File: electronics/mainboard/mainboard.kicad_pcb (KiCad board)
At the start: 2 copper layers, 1 part

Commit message: add terminals
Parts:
- added J1: Conn_01x09, Wuerth:691247510009, F.Cu at (224.5, 118.2)
- added J2: Conn_01x09, Wuerth:691247510009, F.Cu at (209.2, 118.2)

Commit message: place parts
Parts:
- added J3: Conn_01x09, Wuerth:691247510009, F.Cu at (178.8, 91.3)
- added J4: Conn_01x09, Wuerth:691247510009, F.Cu at (163.5, 91.3)
- added J5: Conn_01x09, Wuerth:691247510009, F.Cu at (148.3, 91.3)
- added J6: Conn_01x09, Wuerth:691247510009, F.Cu at (133.1, 91.3)
- added J7: Conn_01x09, Wuerth:691247510009, F.Cu at (117.8, 91.3)
- added J8: Conn_01x09, Wuerth:691247510009, F.Cu at (102.6, 91.3)
- added J9: Conn_01x09, Wuerth:691247510009, F.Cu at (87.3, 91.3)
- added J99: Conn_01x08, Connector_PinHeader_2.54mm:PinHeader_1x08_P2.54mm_Vertical_SMD_Pin1Right, B.Cu at (156.8, 111.1)
- moved XA1 62.0 mm to (97.2, 113.7)
- moved J1 27.6 mm to (218.1, 91.3), turned to 180 degrees
- moved J2 27.6 mm to (202.9, 91.3), turned to 180 degrees
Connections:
- XA1 pad A0: unconnected-(XA1-PadA0) -> Net-(XA1-PadA0)
- XA1 pad A1: unconnected-(XA1-PadA1) -> Net-(XA1-PadA1)
- XA1 pad A2: unconnected-(XA1-PadA2) -> Net-(XA1-PadA2)
- XA1 pad A3: unconnected-(XA1-PadA3) -> Net-(XA1-PadA3)
- XA1 pad A4: unconnected-(XA1-PadA4) -> Net-(XA1-PadA4)
- XA1 pad A5: unconnected-(XA1-PadA5) -> Net-(XA1-PadA5)
- XA1 pad A6: unconnected-(XA1-PadA6) -> Net-(XA1-PadA6)
- XA1 pad A7: unconnected-(XA1-PadA7) -> Net-(XA1-PadA7)
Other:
- board outline added: 151.1 x 55.9 mm

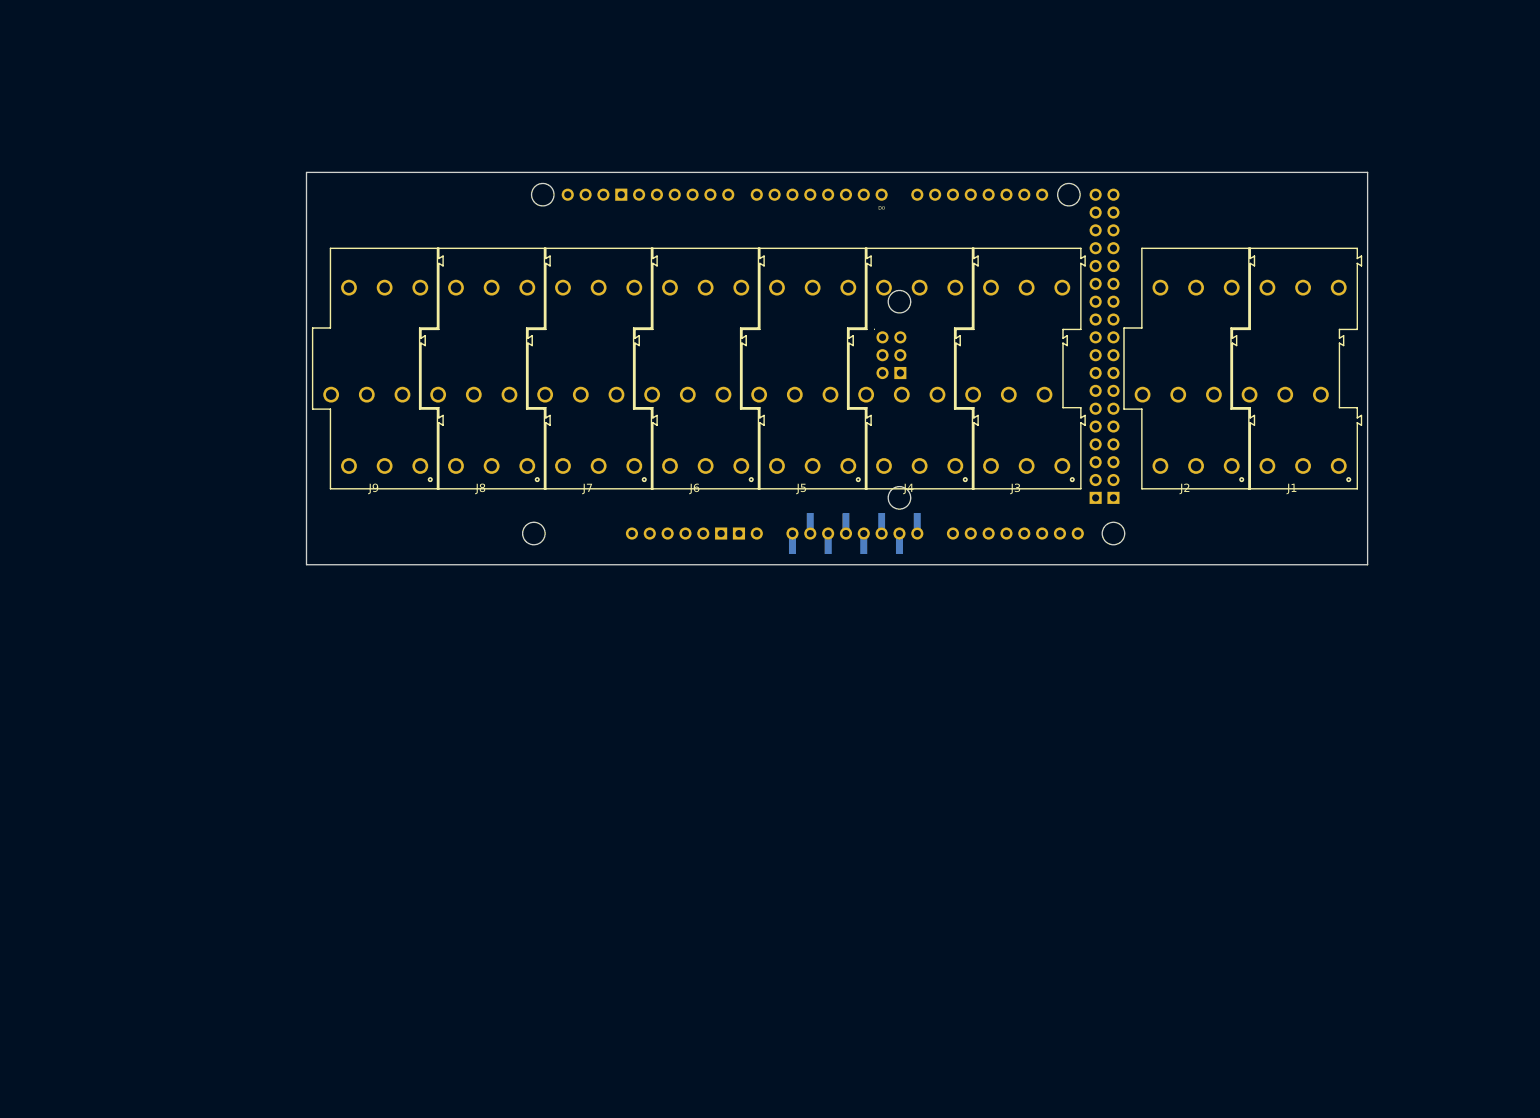
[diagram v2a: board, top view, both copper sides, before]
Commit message: add and wire parts in schematic
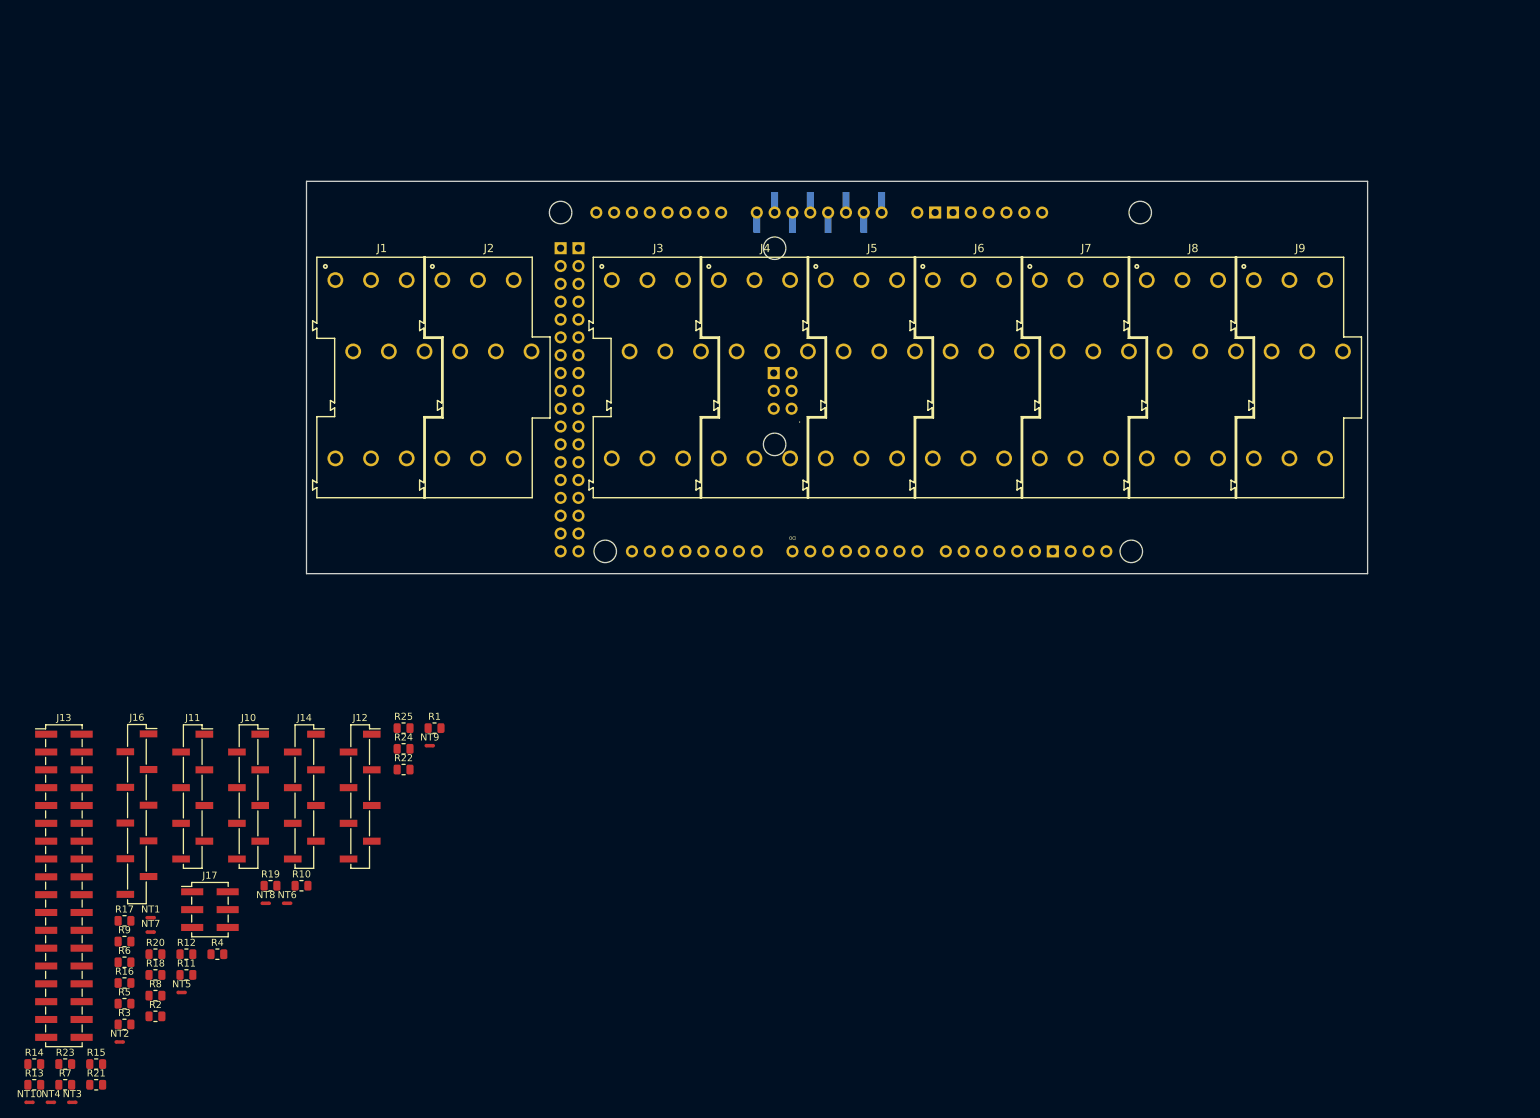
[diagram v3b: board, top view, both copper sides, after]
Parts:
- added J10: Conn_01x08, Connector_PinHeader_2.54mm:PinHeader_1x08_P2.54mm_Vertical_SMD_Pin1Right, F.Cu at (70.5, 148.6)
- added J11: Conn_01x08, Connector_PinHeader_2.54mm:PinHeader_1x08_P2.54mm_Vertical_SMD_Pin1Right, F.Cu at (62.5, 148.6)
- added J12: Conn_01x08, Connector_PinHeader_2.54mm:PinHeader_1x08_P2.54mm_Vertical_SMD_Pin1Right, F.Cu at (86.4, 148.6)
- added J13: Conn_02x18_Odd_Even, Connector_PinHeader_2.54mm:PinHeader_2x18_P2.54mm_Vertical_SMD, F.Cu at (44.2, 161.3)
- added J14: Conn_01x08, Connector_PinHeader_2.54mm:PinHeader_1x08_P2.54mm_Vertical_SMD_Pin1Right, F.Cu at (78.4, 148.6)
- added J16: Conn_01x10, Connector_PinHeader_2.54mm:PinHeader_1x10_P2.54mm_Vertical_SMD_Pin1Right, F.Cu at (54.6, 151.1)
- added J17: Conn_02x03_Odd_Even, Connector_PinHeader_2.54mm:PinHeader_2x03_P2.54mm_Vertical_SMD, F.Cu at (65.0, 164.7)
- added NT1: NetTie_2, NetTie:NetTie-2_SMD_Pad0.5mm, F.Cu at (56.5, 165.8)
- added NT10: NetTie_2, NetTie:NetTie-2_SMD_Pad0.5mm, F.Cu at (39.3, 192.1)
- added NT2: NetTie_2, NetTie:NetTie-2_SMD_Pad0.5mm, F.Cu at (52.1, 183.5)
- added NT3: NetTie_2, NetTie:NetTie-2_SMD_Pad0.5mm, F.Cu at (45.4, 192.1)
- added NT4: NetTie_2, NetTie:NetTie-2_SMD_Pad0.5mm, F.Cu at (42.3, 192.1)
- added NT5: NetTie_2, NetTie:NetTie-2_SMD_Pad0.5mm, F.Cu at (61.0, 176.5)
- added NT6: NetTie_2, NetTie:NetTie-2_SMD_Pad0.5mm, F.Cu at (76.0, 163.8)
- added NT7: NetTie_2, NetTie:NetTie-2_SMD_Pad0.5mm, F.Cu at (56.5, 167.9)
- added NT8: NetTie_2, NetTie:NetTie-2_SMD_Pad0.5mm, F.Cu at (72.9, 163.8)
- added NT9: NetTie_2, NetTie:NetTie-2_SMD_Pad0.5mm, F.Cu at (96.3, 141.3)
- added R1: 0, Resistor_SMD:R_0805_2012Metric, F.Cu at (97.0, 138.8)
- added R10: 0, Resistor_SMD:R_0805_2012Metric, F.Cu at (78.0, 161.3)
- added R11: 0, Resistor_SMD:R_0805_2012Metric, F.Cu at (61.6, 174.0)
- added R12: 0, Resistor_SMD:R_0805_2012Metric, F.Cu at (61.6, 171.0)
- added R13: 0, Resistor_SMD:R_0805_2012Metric, F.Cu at (40.0, 189.6)
- added R14: 0, Resistor_SMD:R_0805_2012Metric, F.Cu at (40.0, 186.7)
- added R15: 0, Resistor_SMD:R_0805_2012Metric, F.Cu at (48.8, 186.7)
- added R16: 0, Resistor_SMD:R_0805_2012Metric, F.Cu at (52.8, 175.1)
- added R17: 0, Resistor_SMD:R_0805_2012Metric, F.Cu at (52.8, 166.3)
- added R18: 0, Resistor_SMD:R_0805_2012Metric, F.Cu at (57.2, 174.0)
- added R19: 0, Resistor_SMD:R_0805_2012Metric, F.Cu at (73.6, 161.3)
- added R2: 0, Resistor_SMD:R_0805_2012Metric, F.Cu at (57.2, 179.9)
- added R20: 0, Resistor_SMD:R_0805_2012Metric, F.Cu at (57.2, 171.0)
- added R21: 0, Resistor_SMD:R_0805_2012Metric, F.Cu at (48.8, 189.6)
- added R22: 0, Resistor_SMD:R_0805_2012Metric, F.Cu at (92.6, 144.7)
- added R23: 0, Resistor_SMD:R_0805_2012Metric, F.Cu at (44.4, 186.7)
- added R24: 0, Resistor_SMD:R_0805_2012Metric, F.Cu at (92.6, 141.8)
- added R25: 0, Resistor_SMD:R_0805_2012Metric, F.Cu at (92.6, 138.8)
- added R3: 0, Resistor_SMD:R_0805_2012Metric, F.Cu at (52.8, 181.0)
- added R4: 0, Resistor_SMD:R_0805_2012Metric, F.Cu at (66.0, 171.0)
- added R5: 0, Resistor_SMD:R_0805_2012Metric, F.Cu at (52.8, 178.1)
- added R6: 0, Resistor_SMD:R_0805_2012Metric, F.Cu at (52.8, 172.2)
- added R7: 0, Resistor_SMD:R_0805_2012Metric, F.Cu at (44.4, 189.6)
- added R8: 0, Resistor_SMD:R_0805_2012Metric, F.Cu at (57.2, 176.9)
- added R9: 0, Resistor_SMD:R_0805_2012Metric, F.Cu at (52.8, 169.2)
- moved J9 134.1 mm to (221.3, 85.2), turned to 0 degrees
- moved J1 127.8 mm to (90.5, 85.2), turned to 0 degrees
- moved XA1 125.1 mm to (211.5, 62.9), turned to 180 degrees
- moved J8 103.7 mm to (206.0, 85.2), turned to 0 degrees
- moved J2 97.4 mm to (105.7, 85.2), turned to 0 degrees
- moved J7 73.2 mm to (190.8, 85.2), turned to 0 degrees
- moved J3 49.3 mm to (129.8, 85.2), turned to 0 degrees
- moved J15 46.0 mm to (151.8, 65.4), turned to 90 degrees
- moved J6 43.0 mm to (175.6, 85.2), turned to 0 degrees
- moved J4 19.5 mm to (145.1, 85.2), turned to 0 degrees
- moved J5 13.5 mm to (160.3, 85.2), turned to 0 degrees
- renumbered J99 to J15
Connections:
- J1 pad 1: unconnected-(J1-Pad1) -> +5V
- J1 pad 2: unconnected-(J1-Pad2) -> /Leds1
- J1 pad 3: unconnected-(J1-Pad3) -> GND
- J1 pad 4: unconnected-(J1-Pad4) -> +5V
- J1 pad 5: unconnected-(J1-Pad5) -> /Leds2
- J1 pad 6: unconnected-(J1-Pad6) -> GND
- J1 pad 7: unconnected-(J1-Pad7) -> +5V
- J1 pad 8: unconnected-(J1-Pad8) -> /Leds3
- J1 pad 9: unconnected-(J1-Pad9) -> GND
- J15 pad 1: Net-(XA1-PadA0) -> /D7
- J15 pad 2: Net-(XA1-PadA1) -> /D6
- J15 pad 3: Net-(XA1-PadA2) -> /D5
- J15 pad 4: Net-(XA1-PadA3) -> /D4
- J15 pad 5: Net-(XA1-PadA4) -> /D3
- J15 pad 6: Net-(XA1-PadA5) -> /D2
- J15 pad 7: Net-(XA1-PadA6) -> /D1
- J15 pad 8: Net-(XA1-PadA7) -> /D0
- J2 pad 1: unconnected-(J2-Pad1) -> +5V
- J2 pad 2: unconnected-(J2-Pad2) -> /Leds4
- J2 pad 3: unconnected-(J2-Pad3) -> GND
- J2 pad 4: unconnected-(J2-Pad4) -> +5V
- J2 pad 5: unconnected-(J2-Pad5) -> /Leds5
- J2 pad 6: unconnected-(J2-Pad6) -> GND
- J2 pad 7: unconnected-(J2-Pad7) -> +5V
- J2 pad 8: unconnected-(J2-Pad8) -> /Leds6
- J2 pad 9: unconnected-(J2-Pad9) -> GND
- J3 pad 1: unconnected-(J3-Pad1) -> +5V
- J3 pad 2: unconnected-(J3-Pad2) -> /Leds7
- J3 pad 3: unconnected-(J3-Pad3) -> GND
- J3 pad 4: unconnected-(J3-Pad4) -> +5V
- J3 pad 5: unconnected-(J3-Pad5) -> /Leds8
- J3 pad 6: unconnected-(J3-Pad6) -> GND
- J3 pad 7: unconnected-(J3-Pad7) -> +5V
- J3 pad 8: unconnected-(J3-Pad8) -> /Leds9
- J3 pad 9: unconnected-(J3-Pad9) -> GND
- J4 pad 1: unconnected-(J4-Pad1) -> +5V
- J4 pad 2: unconnected-(J4-Pad2) -> /Leds10
- J4 pad 3: unconnected-(J4-Pad3) -> GND
- J4 pad 4: unconnected-(J4-Pad4) -> +5V
- J4 pad 5: unconnected-(J4-Pad5) -> /Leds11
- J4 pad 6: unconnected-(J4-Pad6) -> GND
- J4 pad 7: unconnected-(J4-Pad7) -> +5V
- J4 pad 8: unconnected-(J4-Pad8) -> /Leds12
- J4 pad 9: unconnected-(J4-Pad9) -> GND
- J5 pad 1: unconnected-(J5-Pad1) -> +5V
- J5 pad 2: unconnected-(J5-Pad2) -> /Leds13
- J5 pad 3: unconnected-(J5-Pad3) -> GND
- J5 pad 4: unconnected-(J5-Pad4) -> +5V
- J5 pad 5: unconnected-(J5-Pad5) -> /Leds14
- J5 pad 6: unconnected-(J5-Pad6) -> GND
- J5 pad 7: unconnected-(J5-Pad7) -> +5V
- J5 pad 8: unconnected-(J5-Pad8) -> /Leds15
- J5 pad 9: unconnected-(J5-Pad9) -> GND
- J6 pad 1: unconnected-(J6-Pad1) -> +5V
- J6 pad 2: unconnected-(J6-Pad2) -> /Leds16
- J6 pad 3: unconnected-(J6-Pad3) -> GND
- J6 pad 4: unconnected-(J6-Pad4) -> +5V
- J6 pad 5: unconnected-(J6-Pad5) -> /Leds17
- J6 pad 6: unconnected-(J6-Pad6) -> GND
- J6 pad 7: unconnected-(J6-Pad7) -> +5V
- J6 pad 8: unconnected-(J6-Pad8) -> /Leds18
- J6 pad 9: unconnected-(J6-Pad9) -> GND
- J7 pad 1: unconnected-(J7-Pad1) -> +5V
- J7 pad 2: unconnected-(J7-Pad2) -> /Leds19
- J7 pad 3: unconnected-(J7-Pad3) -> GND
- J7 pad 4: unconnected-(J7-Pad4) -> +5V
- J7 pad 5: unconnected-(J7-Pad5) -> /Leds20
- J7 pad 6: unconnected-(J7-Pad6) -> GND
- J7 pad 7: unconnected-(J7-Pad7) -> +5V
- J7 pad 8: unconnected-(J7-Pad8) -> /Leds21
- J7 pad 9: unconnected-(J7-Pad9) -> GND
- J8 pad 1: unconnected-(J8-Pad1) -> +5V
- J8 pad 2: unconnected-(J8-Pad2) -> /Leds22
- J8 pad 3: unconnected-(J8-Pad3) -> GND
- J8 pad 4: unconnected-(J8-Pad4) -> +5V
- J8 pad 5: unconnected-(J8-Pad5) -> /Leds23
- J8 pad 6: unconnected-(J8-Pad6) -> GND
- J8 pad 7: unconnected-(J8-Pad7) -> +5V
- J8 pad 8: unconnected-(J8-Pad8) -> /Leds24
- J8 pad 9: unconnected-(J8-Pad9) -> GND
- J9 pad 1: unconnected-(J9-Pad1) -> +5V
- J9 pad 2: unconnected-(J9-Pad2) -> /Leds25
- J9 pad 3: unconnected-(J9-Pad3) -> GND
- J9 pad 4: unconnected-(J9-Pad4) -> +5V
- J9 pad 6: unconnected-(J9-Pad6) -> GND
- J9 pad 7: unconnected-(J9-Pad7) -> +5V
- J9 pad 9: unconnected-(J9-Pad9) -> GND
- XA1 pad 3V3: unconnected-(XA1-Pad3V3) -> /3V3
- XA1 pad 5V1: unconnected-(XA1-Pad5V1) -> /5V1
- XA1 pad 5V2: unconnected-(XA1-Pad5V2) -> /5V2
- XA1 pad 5V3: unconnected-(XA1-Pad5V3) -> /5V3
- XA1 pad 5V4: unconnected-(XA1-Pad5V4) -> /5V4
- XA1 pad A0: Net-(XA1-PadA0) -> /A0
- XA1 pad A1: Net-(XA1-PadA1) -> /A1
- XA1 pad A10: unconnected-(XA1-PadA10) -> /A10
- XA1 pad A11: unconnected-(XA1-PadA11) -> /A11
- XA1 pad A12: unconnected-(XA1-PadA12) -> /A12
- XA1 pad A13: unconnected-(XA1-PadA13) -> /A13
- XA1 pad A14: unconnected-(XA1-PadA14) -> /A14
- XA1 pad A15: unconnected-(XA1-PadA15) -> /A15
- XA1 pad A2: Net-(XA1-PadA2) -> /A2
- XA1 pad A3: Net-(XA1-PadA3) -> /A3
- XA1 pad A4: Net-(XA1-PadA4) -> /A4
- XA1 pad A5: Net-(XA1-PadA5) -> /A5
- XA1 pad A6: Net-(XA1-PadA6) -> /A6
- XA1 pad A7: Net-(XA1-PadA7) -> /A7
- XA1 pad A8: unconnected-(XA1-PadA8) -> /A8
- XA1 pad A9: unconnected-(XA1-PadA9) -> /A9
- XA1 pad AREF: unconnected-(XA1-PadAREF) -> /AREF
- XA1 pad D0: unconnected-(XA1-PadD0) -> /D0
- XA1 pad D1: unconnected-(XA1-PadD1) -> /D1
- XA1 pad D10: unconnected-(XA1-PadD10) -> /D10
- XA1 pad D11: unconnected-(XA1-PadD11) -> /D11
- XA1 pad D12: unconnected-(XA1-PadD12) -> /D12
- XA1 pad D13: unconnected-(XA1-PadD13) -> /D13
- XA1 pad D14: unconnected-(XA1-PadD14) -> /D14
- XA1 pad D15: unconnected-(XA1-PadD15) -> /D15
- XA1 pad D16: unconnected-(XA1-PadD16) -> /D16
- XA1 pad D17: unconnected-(XA1-PadD17) -> /D17
- XA1 pad D18: unconnected-(XA1-PadD18) -> /D18
- XA1 pad D19: unconnected-(XA1-PadD19) -> /D19
- XA1 pad D2: unconnected-(XA1-PadD2) -> /D2
- XA1 pad D20: unconnected-(XA1-PadD20) -> /D20
- XA1 pad D21: unconnected-(XA1-PadD21) -> /D21
- XA1 pad D22: unconnected-(XA1-PadD22) -> /D22
- XA1 pad D23: unconnected-(XA1-PadD23) -> /D23
- XA1 pad D24: unconnected-(XA1-PadD24) -> /D24
- XA1 pad D25: unconnected-(XA1-PadD25) -> /D25
- XA1 pad D26: unconnected-(XA1-PadD26) -> /D26
- XA1 pad D27: unconnected-(XA1-PadD27) -> /D27
- XA1 pad D28: unconnected-(XA1-PadD28) -> /D28
- XA1 pad D29: unconnected-(XA1-PadD29) -> /D29
- XA1 pad D3: unconnected-(XA1-PadD3) -> /D3
- XA1 pad D30: unconnected-(XA1-PadD30) -> /D30
- XA1 pad D31: unconnected-(XA1-PadD31) -> /D31
- XA1 pad D32: unconnected-(XA1-PadD32) -> /D32
- XA1 pad D33: unconnected-(XA1-PadD33) -> /D33
- XA1 pad D34: unconnected-(XA1-PadD34) -> /D34
- XA1 pad D35: unconnected-(XA1-PadD35) -> /D35
- XA1 pad D36: unconnected-(XA1-PadD36) -> /D36
- XA1 pad D37: unconnected-(XA1-PadD37) -> /D37
- XA1 pad D38: unconnected-(XA1-PadD38) -> /D38
- XA1 pad D39: unconnected-(XA1-PadD39) -> /D39
- XA1 pad D4: unconnected-(XA1-PadD4) -> /D4
- XA1 pad D40: unconnected-(XA1-PadD40) -> /D40
- XA1 pad D41: unconnected-(XA1-PadD41) -> /D41
- XA1 pad D42: unconnected-(XA1-PadD42) -> /D42
- XA1 pad D43: unconnected-(XA1-PadD43) -> /D43
- XA1 pad D44: unconnected-(XA1-PadD44) -> /D44
- XA1 pad D45: unconnected-(XA1-PadD45) -> /D45
- XA1 pad D46: unconnected-(XA1-PadD46) -> /D46
- XA1 pad D47: unconnected-(XA1-PadD47) -> /D47
- XA1 pad D48: unconnected-(XA1-PadD48) -> /D48
- XA1 pad D49: unconnected-(XA1-PadD49) -> /D49
- XA1 pad D5: unconnected-(XA1-PadD5) -> /D5
- XA1 pad D50: unconnected-(XA1-PadD50) -> /D50
- XA1 pad D51: unconnected-(XA1-PadD51) -> /D51
- XA1 pad D52: unconnected-(XA1-PadD52) -> /D52
- XA1 pad D53: unconnected-(XA1-PadD53) -> /D53
- XA1 pad D6: unconnected-(XA1-PadD6) -> /D6
- XA1 pad D7: unconnected-(XA1-PadD7) -> /D7
- XA1 pad D8: unconnected-(XA1-PadD8) -> /D8
- XA1 pad D9: unconnected-(XA1-PadD9) -> /D9
- XA1 pad GND1: unconnected-(XA1-PadGND1) -> /GND1
- XA1 pad GND2: unconnected-(XA1-PadGND2) -> /GND2
- XA1 pad GND3: unconnected-(XA1-PadGND3) -> /GND3
- XA1 pad GND4: unconnected-(XA1-PadGND4) -> /GND4
- XA1 pad GND5: unconnected-(XA1-PadGND5) -> /GND5
- XA1 pad GND6: unconnected-(XA1-PadGND6) -> /GND6
- XA1 pad IORF: unconnected-(XA1-PadIORF) -> /IORF
- XA1 pad MISO: unconnected-(XA1-PadMISO) -> /MISO
- XA1 pad MOSI: unconnected-(XA1-PadMOSI) -> /MOSI
- XA1 pad RST1: unconnected-(XA1-PadRST1) -> /RST1
- XA1 pad RST2: unconnected-(XA1-PadRST2) -> /RST2
- XA1 pad SCK: unconnected-(XA1-PadSCK) -> /SCK
- XA1 pad SCL: unconnected-(XA1-PadSCL) -> /SCL
- XA1 pad SDA: unconnected-(XA1-PadSDA) -> /SDA
- XA1 pad VIN: unconnected-(XA1-PadVIN) -> /VIN

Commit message: place parts on pcb
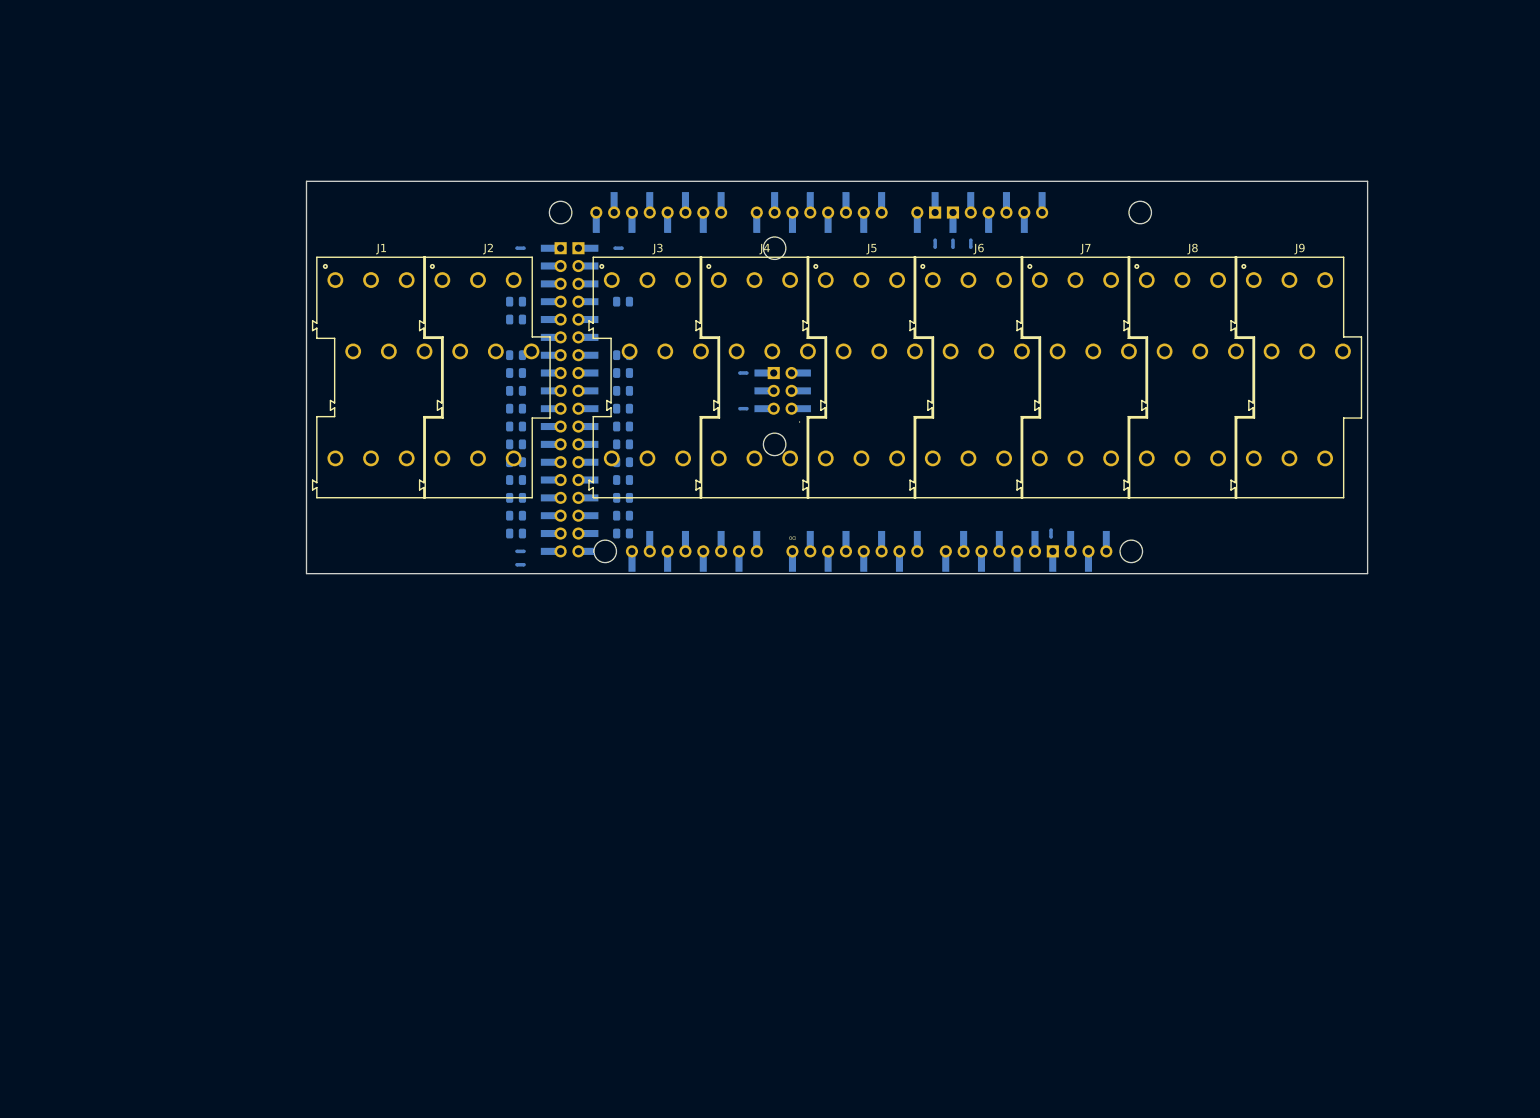
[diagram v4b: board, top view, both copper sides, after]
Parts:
- J10, J11, J12, J13, J14, J16, NT1, NT10, NT2, NT3, NT4, NT5, NT6, NT7, NT8, NT9, R1, R10, R11, R12, R13, R14, R15, R16, R17, R18, R19, R2, R20, R21, R22, R23, R24, R25, R3, R4, R5, R6, R7, R8, R9: moved to B.Cu
- J17: footprint Connector_PinHeader_2.54mm:PinHeader_2x03_P2.54mm_Vertical_SMD -> Connector_PinSocket_2.54mm:PinSocket_2x03_P2.54mm_Vertical_SMD; moved to B.Cu
- moved NT1 151.2 mm to (173.4, 69.8), turned to 90 degrees
- moved NT7 148.6 mm to (168.3, 69.8), turned to 90 degrees
- moved NT10 140.3 mm to (109.2, 70.5)
- moved NT5 140.0 mm to (184.8, 111.1), turned to -90 degrees
- moved NT6 133.5 mm to (170.8, 69.8), turned to 90 degrees
- moved J10 133.3 mm to (174.6, 65.4), turned to 90 degrees
- moved J16 132.1 mm to (181.2, 113.7), turned to 90 degrees
- moved R21 128.2 mm to (123.8, 85.7), turned to 180 degrees
- moved NT2 126.6 mm to (141.0, 93.3)
- moved R13 125.8 mm to (123.8, 95.9), turned to 180 degrees
- moved R23 124.0 mm to (108.6, 80.6)
- moved J11 122.0 mm to (151.8, 65.4), turned to 90 degrees
- moved R15 119.8 mm to (123.8, 93.3), turned to 180 degrees
- moved R7 117.2 mm to (123.8, 103.5), turned to 180 degrees
- moved R14 113.8 mm to (108.6, 95.9)
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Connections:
- J13 pad 1: /5V3 -> /5V4
- J13 pad 10: /D29 -> /D28
- J13 pad 11: /D30 -> /D31
- J13 pad 12: /D31 -> /D30
- J13 pad 13: /D32 -> /D33
- J13 pad 14: /D33 -> /D32
- J13 pad 15: /D34 -> /D35
- J13 pad 16: /D35 -> /D34
- J13 pad 17: /D36 -> /D37
- J13 pad 18: /D37 -> /D36
- J13 pad 19: /D38 -> /D39
- J13 pad 2: /5V4 -> /5V3
- J13 pad 20: /D39 -> /D38
- J13 pad 21: /D40 -> /D41
- J13 pad 22: /D41 -> /D40
- J13 pad 23: /D42 -> /D43
- J13 pad 24: /D43 -> /D42
- J13 pad 25: /D44 -> /D45
- J13 pad 26: /D45 -> /D44
- J13 pad 27: /D46 -> /D47
- J13 pad 28: /D47 -> /D46
- J13 pad 29: /D48 -> /D49
- J13 pad 3: /D22 -> /D23
- J13 pad 30: /D49 -> /D48
- J13 pad 31: /D50 -> /D51
- J13 pad 32: /D51 -> /D50
- J13 pad 33: /D52 -> /D53
- J13 pad 34: /D53 -> /D52
- J13 pad 35: /GND5 -> /GND6
- J13 pad 36: /GND6 -> /GND5
- J13 pad 4: /D23 -> /D22
- J13 pad 5: /D24 -> /D25
- J13 pad 6: /D25 -> /D24
- J13 pad 7: /D26 -> /D27
- J13 pad 8: /D27 -> /D26
- J13 pad 9: /D28 -> /D29

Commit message: route pcb
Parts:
- removed NT10: NetTie_2, NetTie:NetTie-2_SMD_Pad0.5mm
- NT1, NT2, NT3, NT7: footprint NetTie:NetTie-2_SMD_Pad0.5mm -> NetTie:NetTie-2_SMD_Pad2.0mm; moved to F.Cu
- NT4, NT5, NT6, NT8, NT9: footprint NetTie:NetTie-2_SMD_Pad0.5mm -> NetTie:NetTie-2_SMD_Pad2.0mm
- moved R25 78.2 mm to (186.7, 82.5), turned to 180 degrees
- moved NT4 75.8 mm to (185.0, 111.7), turned to -90 degrees
- moved R1 71.9 mm to (58.4, 81.3), turned to 0 degrees
- moved R23 67.2 mm to (174.0, 95.9), turned to 180 degrees
- moved R3 65.4 mm to (58.4, 106.7), turned to 0 degrees
- moved R22 63.0 mm to (171.4, 81.3), turned to 180 degrees
- moved R24 55.5 mm to (171.4, 106.7)
- moved R2 51.5 mm to (61.0, 91.4)
- moved R20 50.6 mm to (158.8, 94.6), turned to 180 degrees
- moved R5 50.2 mm to (76.2, 90.2), turned to 0 degrees
- moved NT5 45.9 mm to (170.8, 67.4), turned to 90 degrees
- moved R4 45.1 mm to (73.7, 80.0)
- moved R7 42.8 mm to (88.9, 78.7), turned to 0 degrees
- moved J4 40.6 mm to (104.4, 85.2)
- moved J3 40.6 mm to (89.2, 85.2)
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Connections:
- NT3 pad 2: /5V3 -> /5V4
- NT4 pad 1: +5V -> GND
- NT4 pad 2: /5V4 -> /GND1
- NT5 pad 2: /GND1 -> /GND2
- NT6 pad 2: /GND2 -> /GND3
- NT7 pad 2: /GND3 -> /GND4
- NT8 pad 2: /GND4 -> /GND5
- NT9 pad 2: /GND5 -> /GND6
- R1 pad 2: /D22 -> /D45
- R10 pad 2: /D31 -> /D51
- R11 pad 2: /D32 -> /D41
- R12 pad 2: /D33 -> /D29
- R13 pad 2: /D34 -> /D50
- R14 pad 2: /D35 -> /D40
- R15 pad 2: /D36 -> /D28
- R16 pad 2: /D37 -> /D48
- R18 pad 2: /D39 -> /D26
- R19 pad 2: /D40 -> /D46
- R2 pad 2: /D23 -> /D35
- R20 pad 2: /D41 -> /D36
- R21 pad 2: /D42 -> /D24
- R22 pad 2: /D43 -> /D44
- R23 pad 2: /D47 -> /D34
- R24 pad 2: /D48 -> /D22
- R25 pad 2: /D49 -> /D42
- R3 pad 2: /D24 -> /D23
- R4 pad 2: /D25 -> /D47
- R5 pad 2: /D26 -> /D37
- R6 pad 2: /D27 -> /D25
- R7 pad 2: /D28 -> /D49
- R8 pad 2: /D29 -> /D39
- R9 pad 2: /D30 -> /D27
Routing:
- net /D42: track 0.00 -> 72.2 mm
- net /D23: track 0.00 -> 57.4 mm
- net /D45: track 0.00 -> 56.4 mm
- net /D34: track 0.00 -> 55.6 mm
- net /D35: track 0.00 -> 54.9 mm
- net /D44: track 0.00 -> 53.9 mm
- net /D22: track 0.00 -> 53.6 mm
- net /D25: track 0.00 -> 41.7 mm
- net /D36: track 0.00 -> 40.9 mm
- net /D47: track 0.00 -> 40.6 mm
- net /D24: track 0.00 -> 39.1 mm
- net /D37: track 0.00 -> 39.1 mm
- net /D46: track 0.00 -> 38.1 mm
- net /D27: track 0.00 -> 25.9 mm
- net /D49: track 0.00 -> 25.4 mm
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- added copper zone on F.Cu, net +5V
- added copper zone on B.Cu, net GND
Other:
- board size 151.1 x 55.9 mm -> 151.8 x 54.6 mm
